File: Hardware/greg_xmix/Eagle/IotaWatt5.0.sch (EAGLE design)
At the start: 66 parts, among them J0 2.1MMJACKSMT, J1 STEREO_SMD, J10 STEREO_SMD, J11 STEREO_SMD, J12 STEREO_SMD, J13 STEREO_SMD, J14 STEREO_SMD, J15 2.1MMJACKSMT, J16 2.1MMJACKSMT, J2 STEREO_SMD, J3 STEREO_SMD, J4 STEREO_SMD, J5 STEREO_SMD, J6 STEREO_SMD, J7 STEREO_SMD, J8 STEREO_SMD, J9 STEREO_SMD, Y1 32Khz

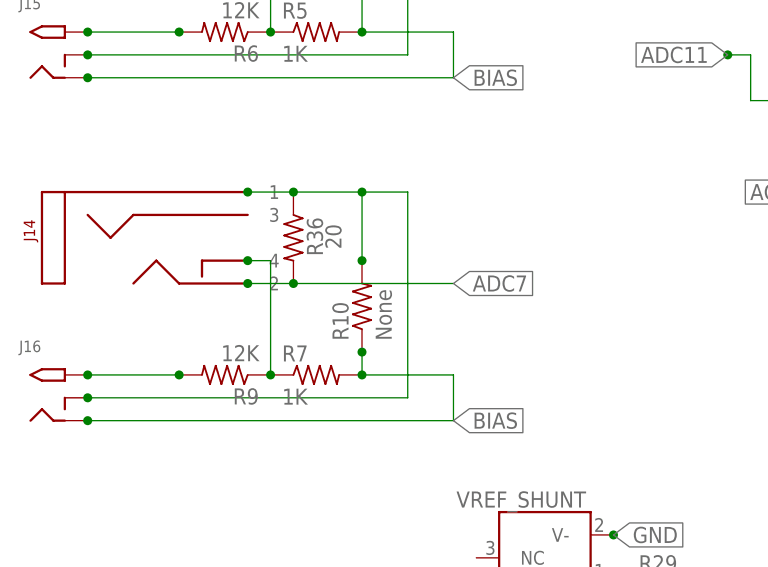
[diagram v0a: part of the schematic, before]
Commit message: added LCSC part numbers
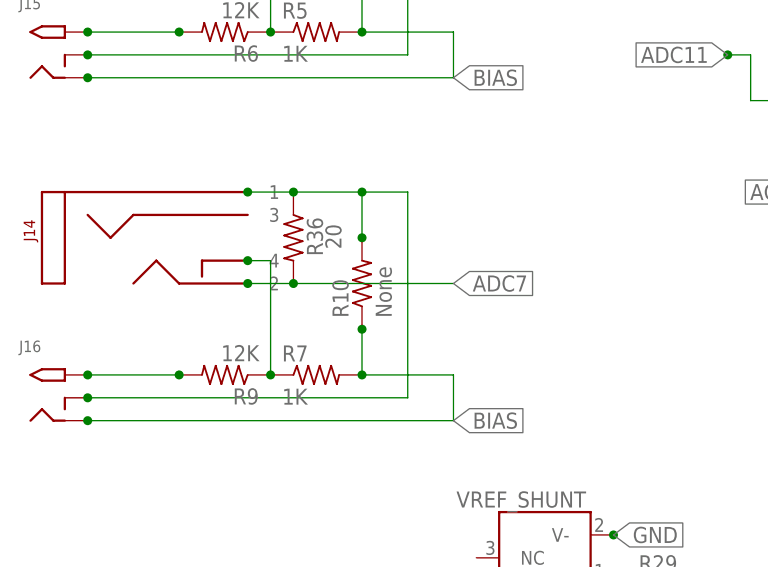
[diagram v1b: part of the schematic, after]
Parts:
- C1, C2, C7: LCSC_PART (none) -> C15850
- C3, C4, C5, C6: LCSC_PART (none) -> C49678
- R1, R2: LCSC_PART (none) -> C515732
- R10, R11: LCSC_PART (none) -> C17477
- R12, R16, R20, R24, R28, R36, R40, R44, R48, R52, R56, R57, R58, R8: LCSC_PART (none) -> C723660
- R29, R3, R31, R5, R7: LCSC_PART (none) -> C309081
- R32, R6, R9: LCSC_PART (none) -> C515719
- R4: LCSC_PART (none) -> C17557
- U$1, U$2: LCSC_PART (none) -> C16939
- U$17, U$19, U$20, U$21: LCSC_PART (none) -> C531179
- U$22: LCSC_PART (none) -> C5423
- U$4: LCSC_PART (none) -> C2651516
- Y1: LCSC_PART (none) -> C179637
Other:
- moved on the sheet: R10
